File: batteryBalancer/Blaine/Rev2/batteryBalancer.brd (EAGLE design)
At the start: 101.6 x 101.6 mm, 50 parts

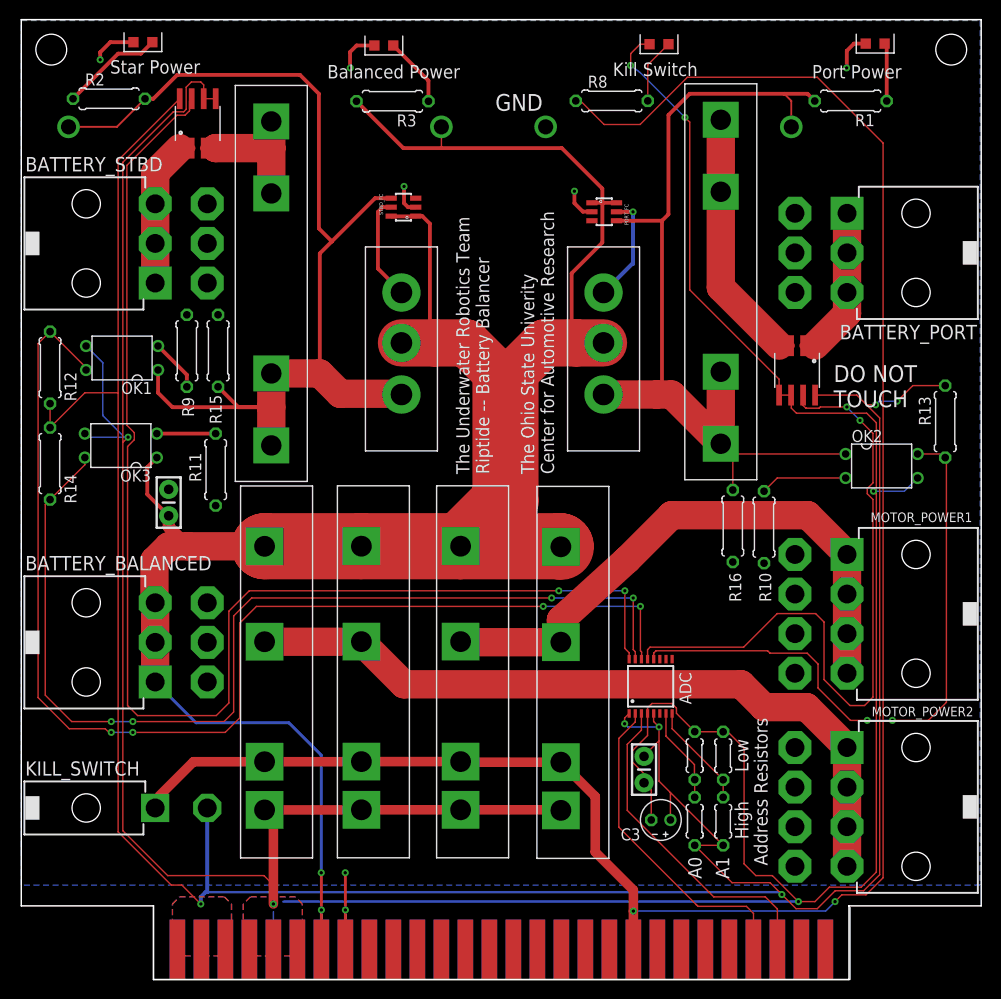
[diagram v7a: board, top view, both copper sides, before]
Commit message: Added water mark and fixed the .6 mm blunder
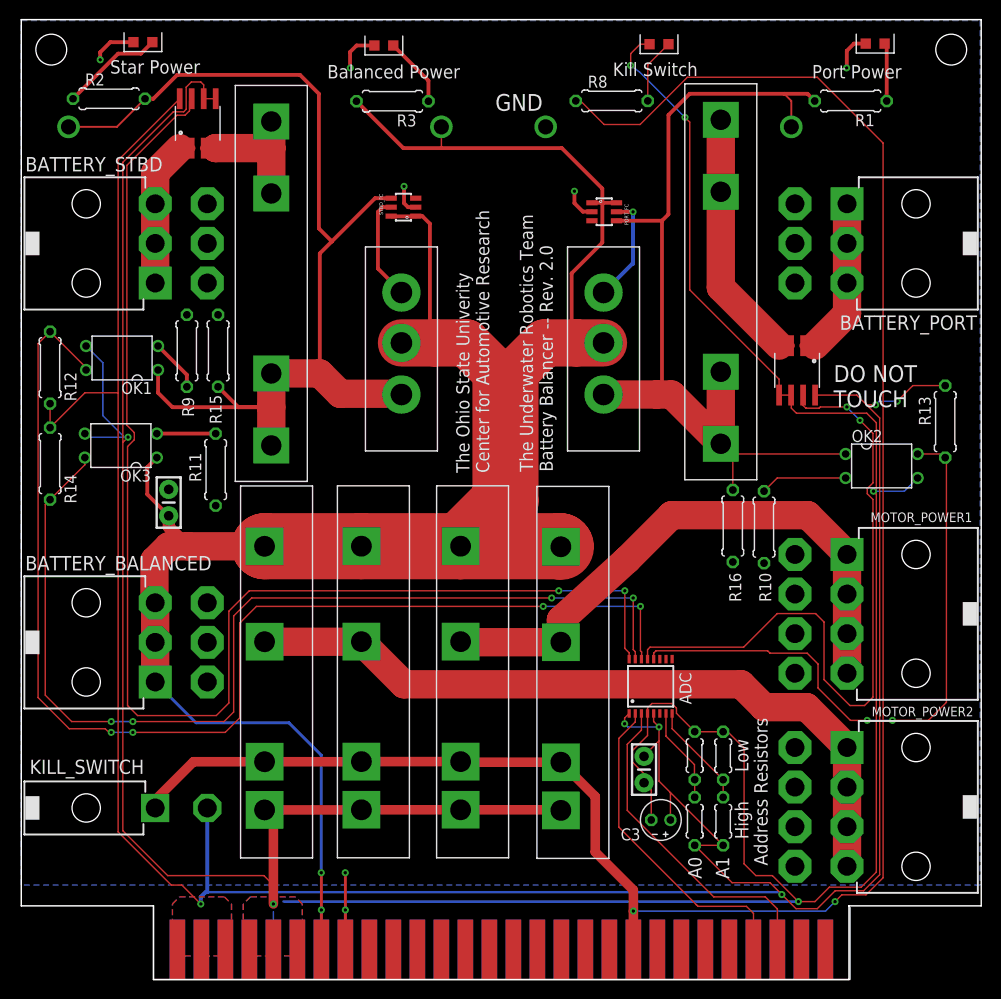
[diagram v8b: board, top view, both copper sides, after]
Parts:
- moved BATTERY_PORT 1.00 mm to (87.4, 77.9)
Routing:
- net PORT_POWER: track 16.7 -> 17.7 mm
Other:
- board text added: "The Underwater Robotics Team Battery Balancer -- Rev. 2.0"
- board text removed: "The Underwater Robotics Team Riptide -- Battery Balancer"
